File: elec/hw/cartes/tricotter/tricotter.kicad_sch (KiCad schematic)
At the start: 66 parts, among them J1 XT60PW-M, J2 3-794618-4, J3 3-794618-4, J4 3-794618-4, J5 3-794618-4, J6 3-794618-4, J7 22272041, Q1 2N7002, Q10 G120P06M, Q2 G120P06M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

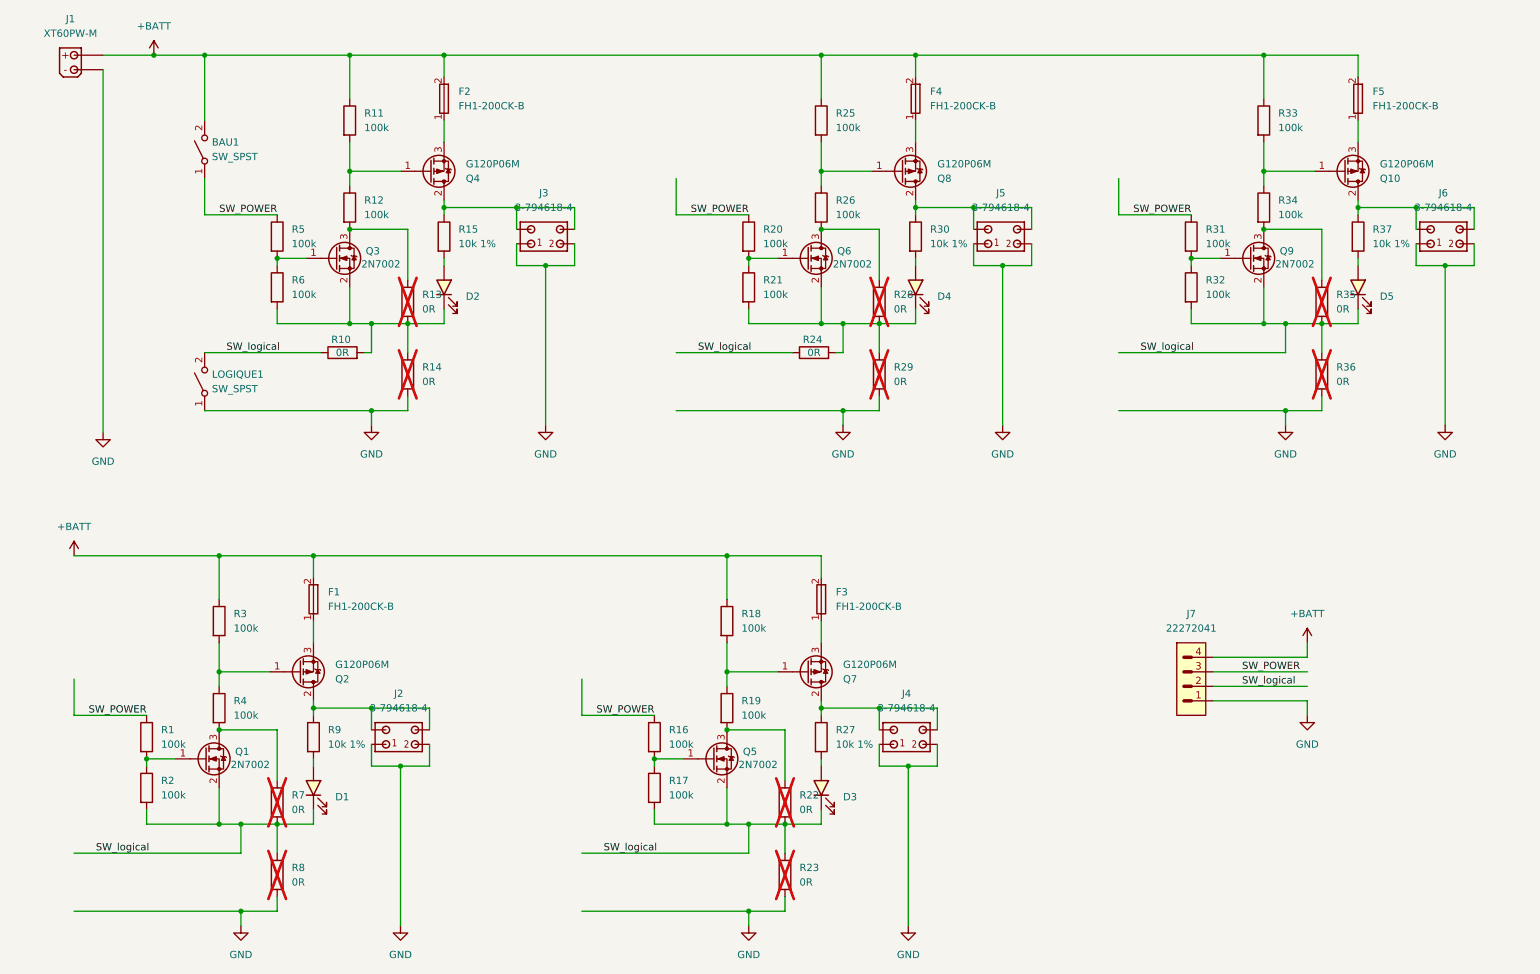
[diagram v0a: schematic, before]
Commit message: tricotter board routed
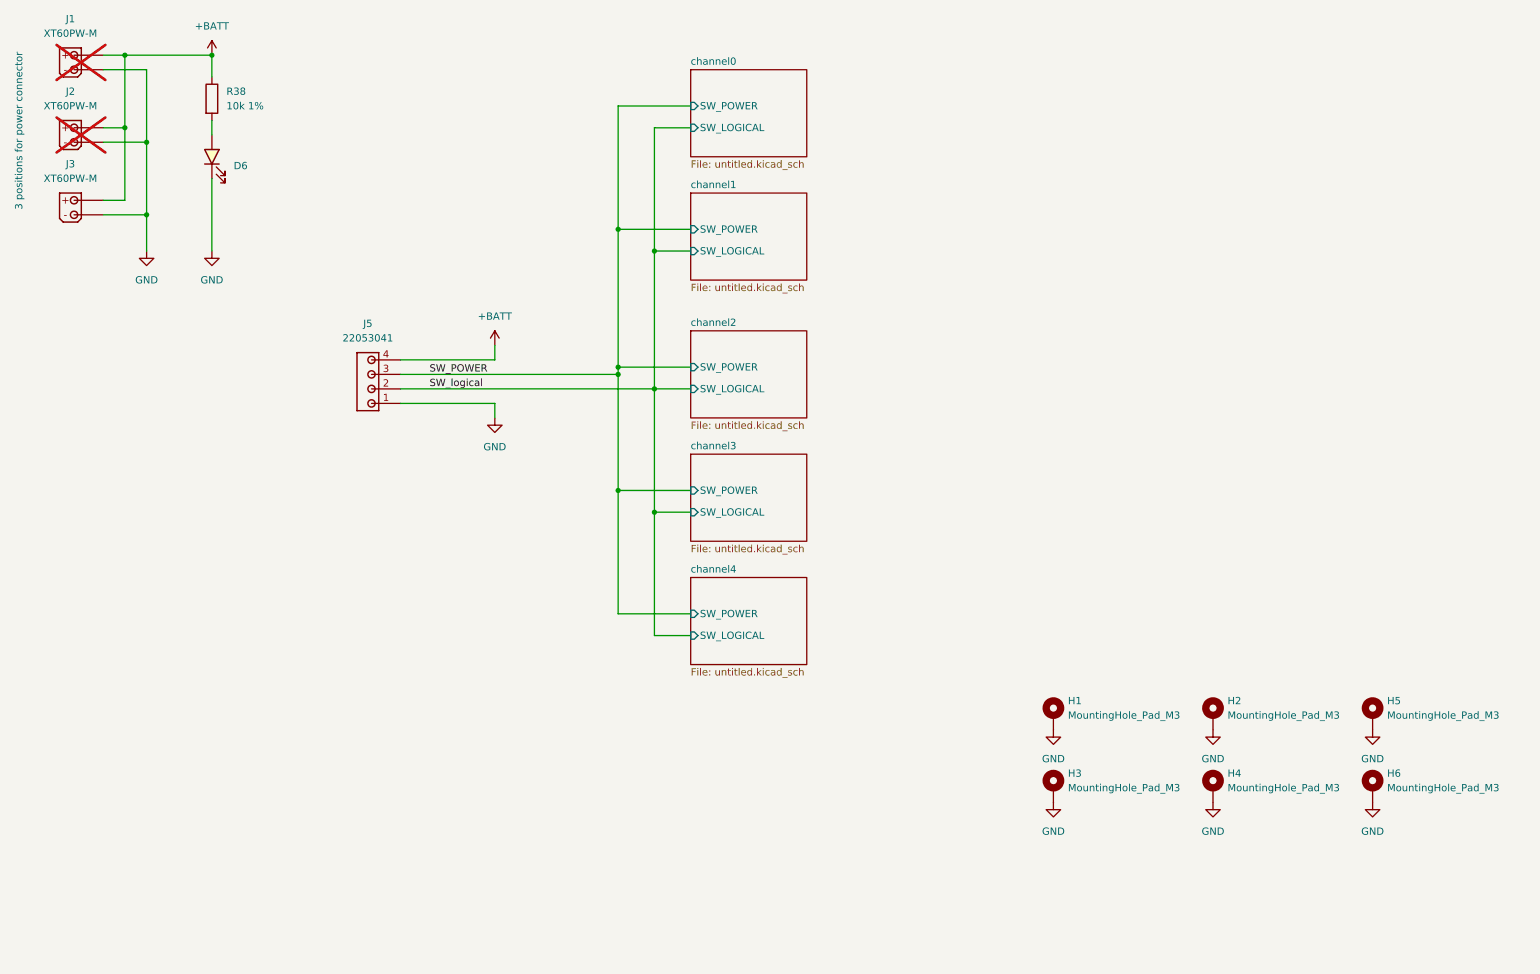
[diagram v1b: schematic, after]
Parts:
- removed BAU1, LOGIQUE1: SW_SPST, symbol Switch:SW_SPST
- removed D1, D2, D3, D4, D5: green, 0603, cocotter_diodes:LED_0603_1608Metric, symbol cocotter_diodes:green_led_0603
- removed F1, F2, F3, F4, F5: FH1-200CK-B, cocotter_others:FUSEHOLDER_5x20mm, symbol cocotter_others:FH1-200CK-B
- removed J2, J3, J4, J5, J6: 3-794618-4, cocotter_connectors:3-794618-4, symbol cocotter_connectors:3-794618-4
- removed J7: 22272041, cocotter_connectors:22272041, symbol cocotter_connectors:22272041
- removed Q1, Q3, Q5, Q6, Q9: 2N7002, cocotter_transistors:SOT-23-3, symbol cocotter_transistors:2N7002
- removed Q10, Q2, Q4, Q7, Q8: G120P06M, cocotter_transistors:TO-263-2-GOFORD, symbol cocotter_transistors:G120P06M
- removed R1, R11, R12, R16, R17, R18, R19, R2, R20, R21, R25, R26, R3, R31, R32, R33, R34, R4, R5, R6: 100k, cocotter_resistor:r0603_reflow, symbol cocotter_resistors:R_100k_0603_1%
- removed R10, R13, R14, R22, R23, R24, R28, R29, R35, R36, R7, R8: 0R, cocotter_resistor:r0603_reflow, symbol cocotter_resistors:R_0R_0603
- removed R15, R27, R30, R37, R9: 10k 1%, cocotter_resistor:r0603_reflow, symbol cocotter_resistors:R_10k_0603_1%
- added D6: white, 0603, cocotter_diodes:LED_0603_1608Metric, symbol cocotter_diodes:white_led_0603
- added H1, H2, H3, H4, H5, H6: MountingHole_Pad_M3, cocotter_others:MountingHole_3.2mm_M3_Pad_Via, symbol cocotter_others:MountingHole_Pad_M3
- added J2, J3: XT60PW-M, cocotter_connectors:XT60PW-M, symbol cocotter_connectors:XT60PW-M
- added J5: 22053041, cocotter_connectors:22053041, symbol cocotter_connectors:22053041
- added R38: 10k 1%, cocotter_resistor:r0603_reflow, symbol cocotter_resistors:R_10k_0603_1%
- J1: now not fitted
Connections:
- net +BATT: now also J2.P, J3.P, J5.4, R38.1
- net GND: now also D6.C, H1.1, H2.1, H3.1, H4.1, H5.1, H6.1, J2.M, J3.M, J5.1
- net SW_POWER: now also J5.3
- net SW_logical: now also J5.2
- new net: D6.A, R38.2
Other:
- added sheet channel0 (untitled.kicad_sch)
- added sheet channel1 (untitled.kicad_sch)
- added sheet channel2 (untitled.kicad_sch)
- added sheet channel3 (untitled.kicad_sch)
- added sheet channel4 (untitled.kicad_sch)
- note added: "3 positions for power connector"
